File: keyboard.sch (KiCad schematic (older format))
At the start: 16 parts, among them IC1 ATMEGA32U4, J1 MINI, X1 ASX3F

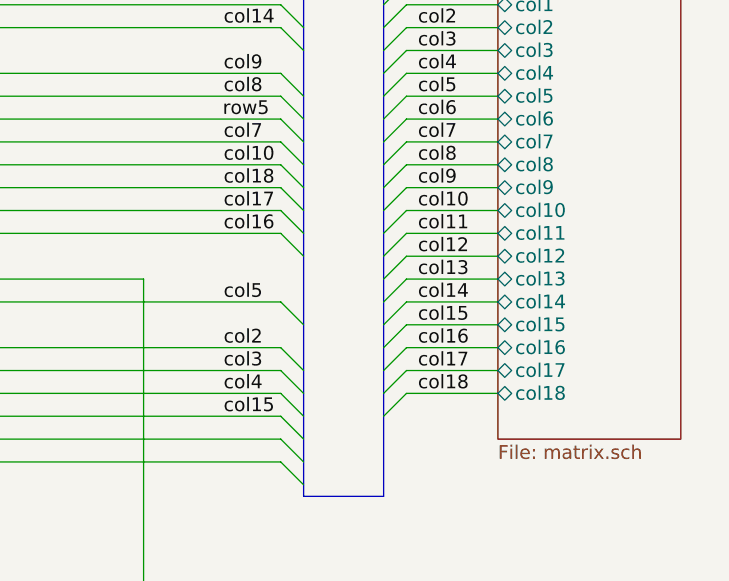
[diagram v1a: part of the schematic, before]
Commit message: PCB with 3 pins ready for backlight
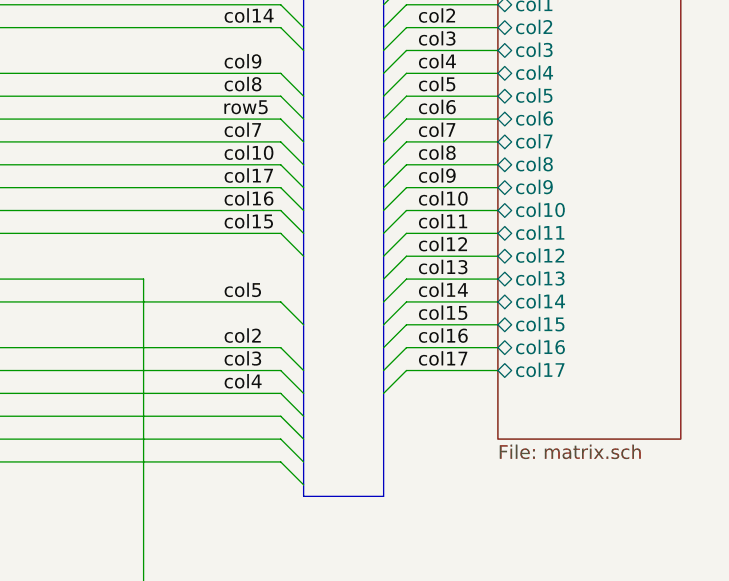
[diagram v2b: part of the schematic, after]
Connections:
- net col18 is gone; now on net col17: IC1.20 ((RXD1/INT2)PD2)
- net col15: now also IC1.18 ((OC0B/SCL/INT0)PD0); no longer IC1.39 ((ADC4/TCK)PF4)
- net col16: now also IC1.19 ((SDA/INT1)PD1); no longer IC1.18 ((OC0B/SCL/INT0)PD0)
- net col17: no longer IC1.19 ((SDA/INT1)PD1)
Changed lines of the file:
@@
 F22 "col16" T L 7050 5850 60
 F23 "col17" T L 7050 5950 60
-F24 "col18" T L 7050 6050 60
 $EndSheet
 Entry Wire Line
@@
 Text Label 5850 4450 0    60   ~ 0
 col14
-Text Label 5850 5150 0    60   ~ 0
-col18
 Text Label 5850 5250 0    60   ~ 0
-col17
+col16
 Text Label 5850 5350 0    60   ~ 0
-col16
-Text Label 5850 6150 0    60   ~ 0
 col15
 Entry Wire Line
 	6550 6050 6650 5950
 Entry Wire Line
-	6550 6150 6650 6050
-Entry Wire Line
 	6550 4550 6650 4450
 Entry Wire Line
@@
 Wire Wire Line
 	6650 5950 7050 5950
-Wire Wire Line
-	6650 6050 7050 6050
 Text Label 6700 5950 0    60   ~ 0
 col17
-Text Label 6700 6050 0    60   ~ 0
-col18
 Text Label 6700 4350 0    60   ~ 0
 col1
@@
 col2
 Wire Bus Line
+	6550 2950 6550 6500
+Wire Bus Line
 	6200 3300 6200 6500
-Wire Bus Line
-	6550 2950 6550 6500
+Text Label 5850 5150 0    60   ~ 0
+col17
 $EndSCHEMATC

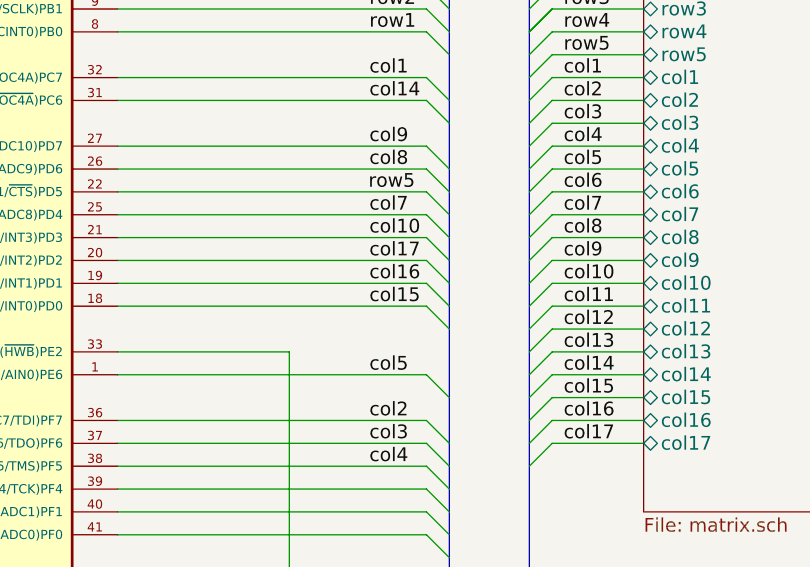
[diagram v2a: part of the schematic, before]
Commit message: Add all keys in PCB for numpad
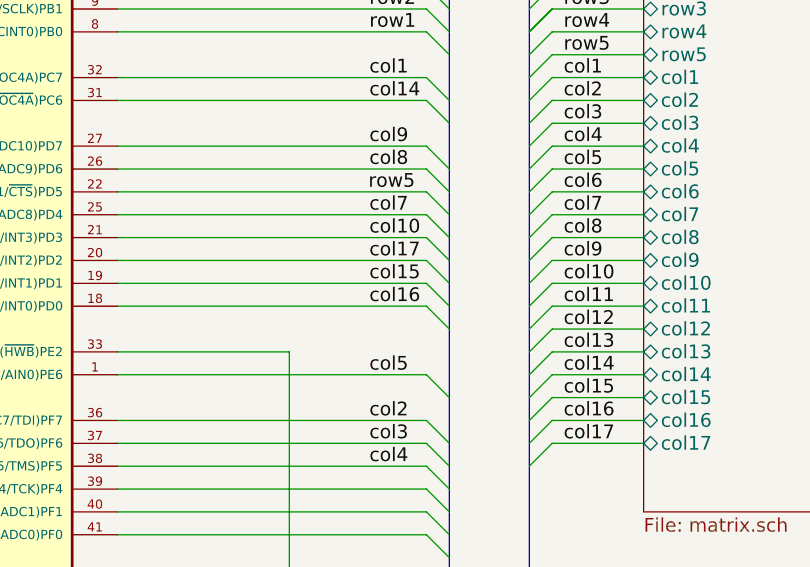
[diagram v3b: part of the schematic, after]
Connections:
- net col15: now also IC1.19 ((SDA/INT1)PD1); no longer IC1.18 ((OC0B/SCL/INT0)PD0)
- net col16: now also IC1.18 ((OC0B/SCL/INT0)PD0); no longer IC1.19 ((SDA/INT1)PD1)
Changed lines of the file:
@@
 col14
 Text Label 5850 5250 0    60   ~ 0
+col15
+Text Label 5850 5350 0    60   ~ 0
 col16
-Text Label 5850 5350 0    60   ~ 0
-col15
 Entry Wire Line
 	6550 6050 6650 5950

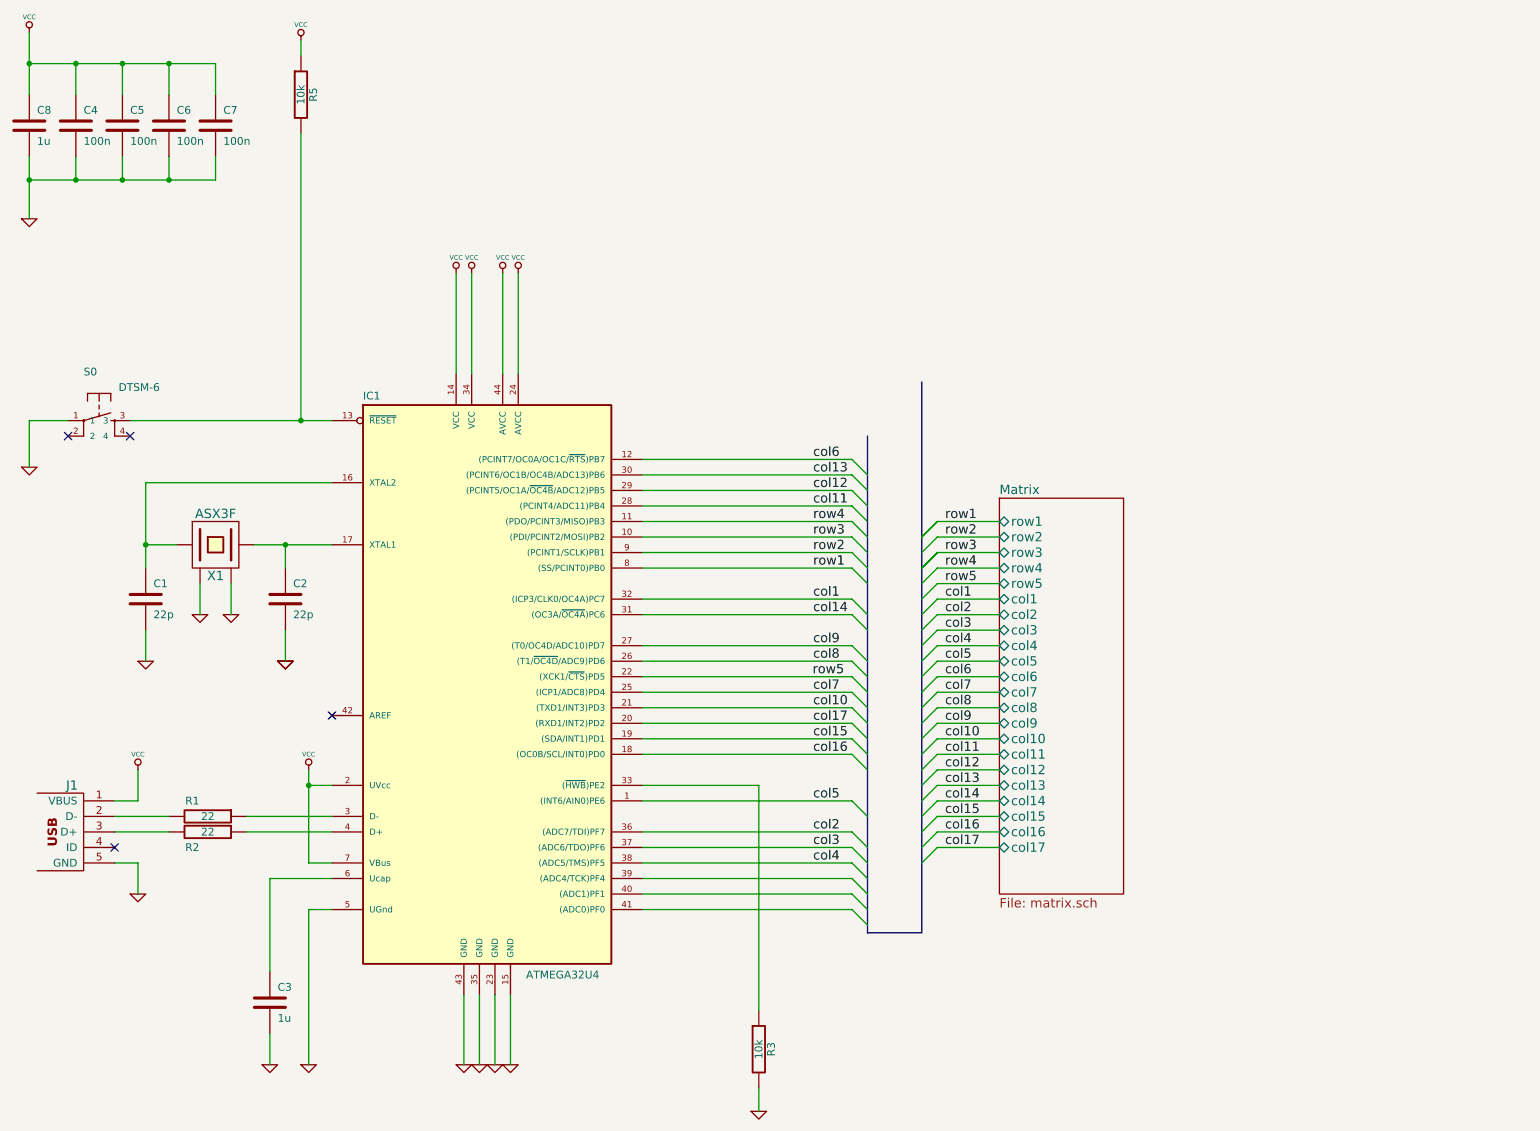
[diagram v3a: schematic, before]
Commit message: Update schematic with USB C receptacle
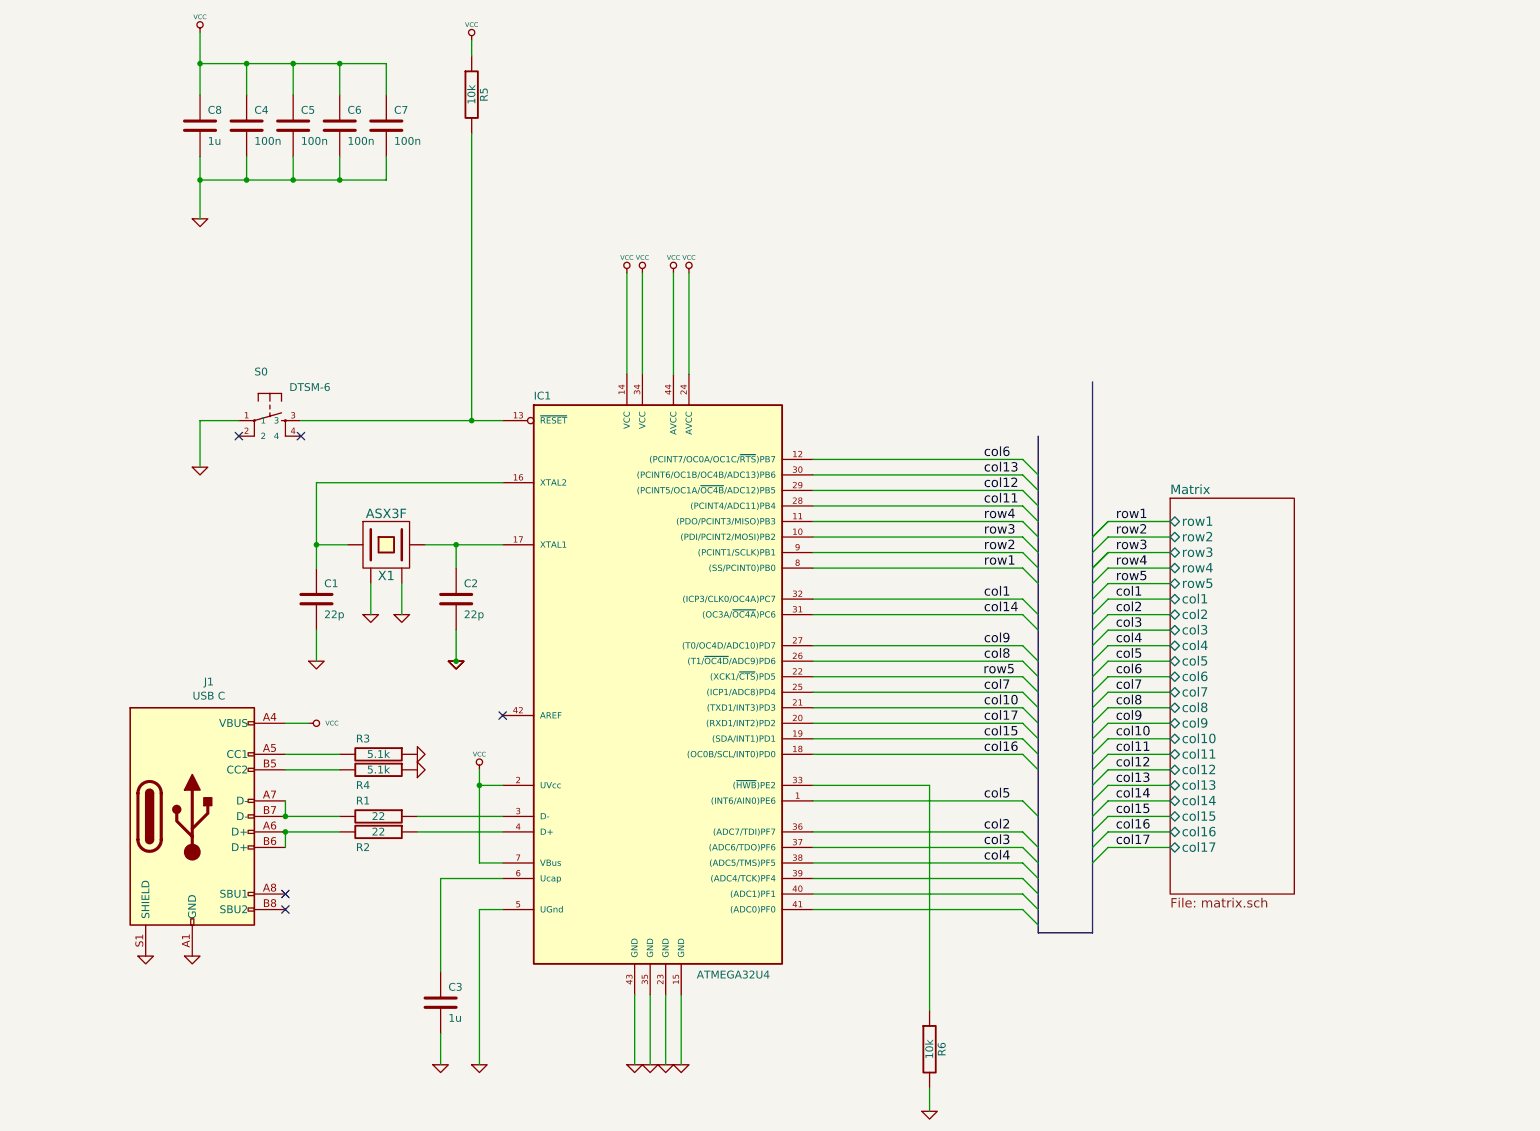
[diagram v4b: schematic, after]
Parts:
- removed J1: MINI, usb:67503, symbol oupiin_usb:USBMINI_B05
- added J1: USB C, symbol Connector:USB_C_Receptacle_USB2.0
- added R3, R4: 5.1k, 0805:0805R, symbol device:R
- renumbered R3 to R6
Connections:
- net GND: now also J1.A1 (GND), J1.A12 (GND), J1.B1 (GND), J1.B12 (GND), J1.S1 (SHIELD), R3.1, R4.1
- net VCC: now also J1.A4 (VBUS), J1.A9 (VBUS), J1.B4 (VBUS), J1.B9 (VBUS)
- net at R1.2: now also J1.A7 (D-), J1.B7 (D-)
- net at R2.2: now also J1.A6 (D+), J1.B6 (D+)
- new net: J1.A5 (CC1), R3.2
- new net: J1.B5 (CC2), R4.2
- no-connect marks 4 -> 5
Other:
- moved on the sheet: C1, C2, C3, C4, C5, C6, C7, C8, IC1, R1, R2, R5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

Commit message: Assign footprint to USB C
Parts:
- J1: footprint (none) -> Connector_USB:USB_C_Receptacle_GCT_USB4085
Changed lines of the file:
@@
 F 0 "J1" H 1957 6617 50  0000 C CNN
 F 1 "USB C" H 1957 6526 50  0000 C CNN
-F 2 "" H 2000 5750 50  0001 C CNN
+F 2 "Connector_USB:USB_C_Receptacle_GCT_USB4085" H 2000 5750 50  0001 C CNN
 F 3 "https://www.usb.org/sites/default/files/documents/usb_type-c.zip" H 2000 5750 50  0001 C CNN
 	1    1850 5750

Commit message: Update PCB to use USB Type C
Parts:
- J1: footprint Connector_USB:USB_C_Receptacle_GCT_USB4085 -> Connector_USB:USB_C_Receptacle_Palconn_UTC16-G
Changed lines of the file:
@@
 F 0 "J1" H 1957 6617 50  0000 C CNN
 F 1 "USB C" H 1957 6526 50  0000 C CNN
-F 2 "Connector_USB:USB_C_Receptacle_GCT_USB4085" H 2000 5750 50  0001 C CNN
+F 2 "Connector_USB:USB_C_Receptacle_Palconn_UTC16-G" H 2000 5750 50  0001 C CNN
 F 3 "https://www.usb.org/sites/default/files/documents/usb_type-c.zip" H 2000 5750 50  0001 C CNN
 	1    1850 5750

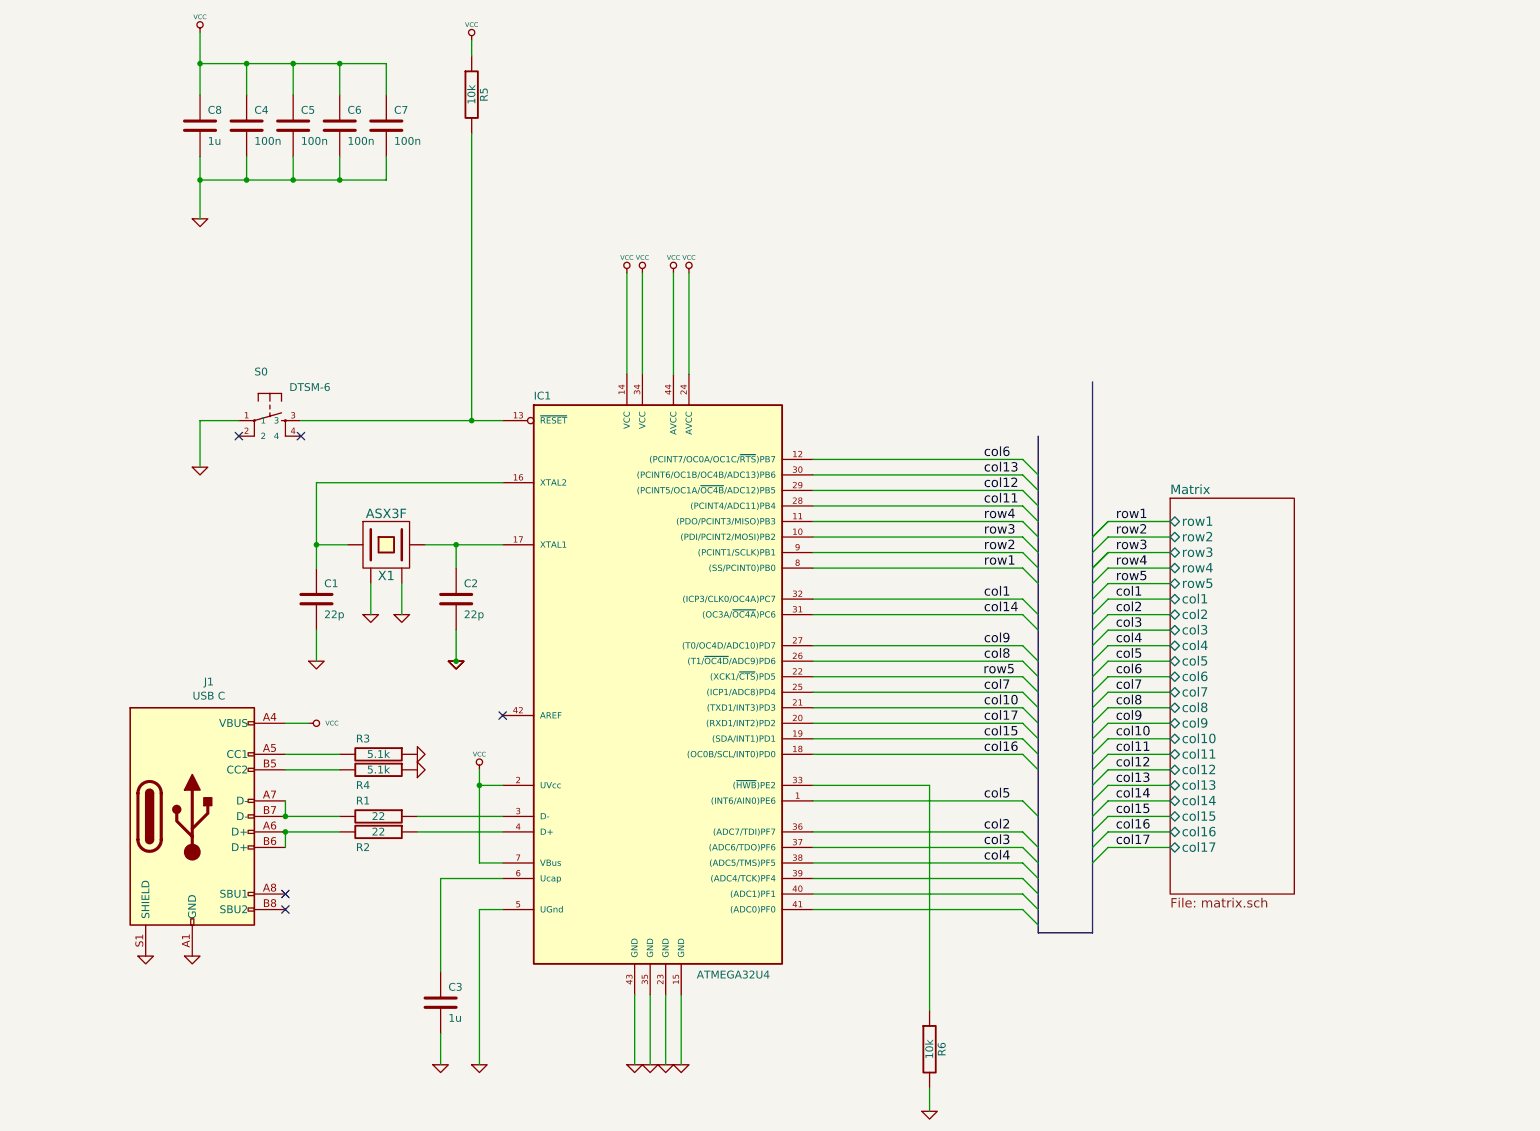
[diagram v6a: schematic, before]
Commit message: Add leds to schematic
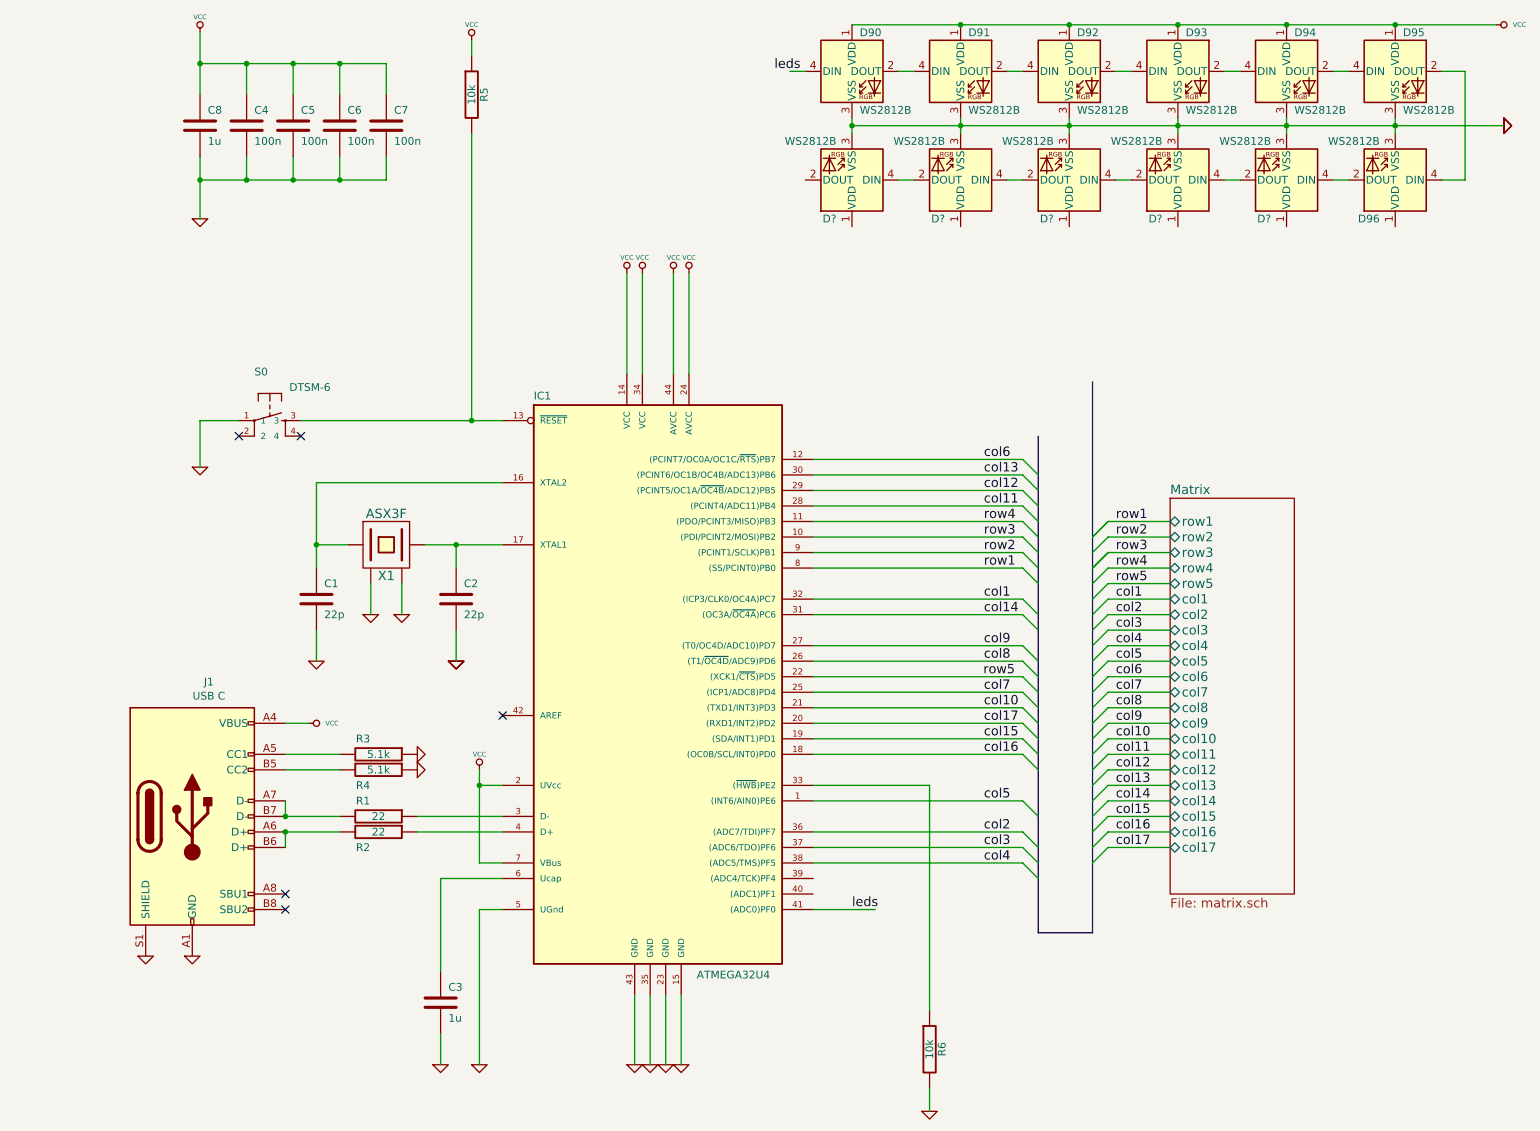
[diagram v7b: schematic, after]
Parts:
- added D90, D91, D92, D93, D94, D95, D96, D? (x5): WS2812B, LED_SMD:LED_WS2812B_PLCC4_5.0x5.0mm_P3.2mm, symbol LED:WS2812B
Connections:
- net GND: now also D90.3 (VSS), D91.3 (VSS), D92.3 (VSS), D93.3 (VSS), D94.3 (VSS), D95.3 (VSS), D96.3 (VSS), D?.3 (VSS), D?.3 (VSS), D?.3 (VSS), D?.3 (VSS), D?.3 (VSS)
- net VCC: now also D90.1 (VDD), D91.1 (VDD), D92.1 (VDD), D93.1 (VDD), D94.1 (VDD), D95.1 (VDD)
- net leds: now reaches IC1.41 ((ADC0)PF0)
- new net: D90.2 (DOUT), D91.4 (DIN)
- new net: D91.2 (DOUT), D92.4 (DIN)
- new net: D92.2 (DOUT), D93.4 (DIN)
- new net: D93.2 (DOUT), D94.4 (DIN)
- new net: D94.2 (DOUT), D95.4 (DIN)
- new net: D95.2 (DOUT), D96.4 (DIN)
- new net: D96.2 (DOUT), D?.4 (DIN)
- new net: D?.2 (DOUT), D?.4 (DIN) (x4)
